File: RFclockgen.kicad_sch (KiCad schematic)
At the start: 13 parts, among them J1 Conn_01x04_Pin, J3 Conn_01x02_Pin, U2 ESP32-S3-WROOM-1, U3 AP2112K-3.3, U4 ESP32-C6-WROOM-1-N8

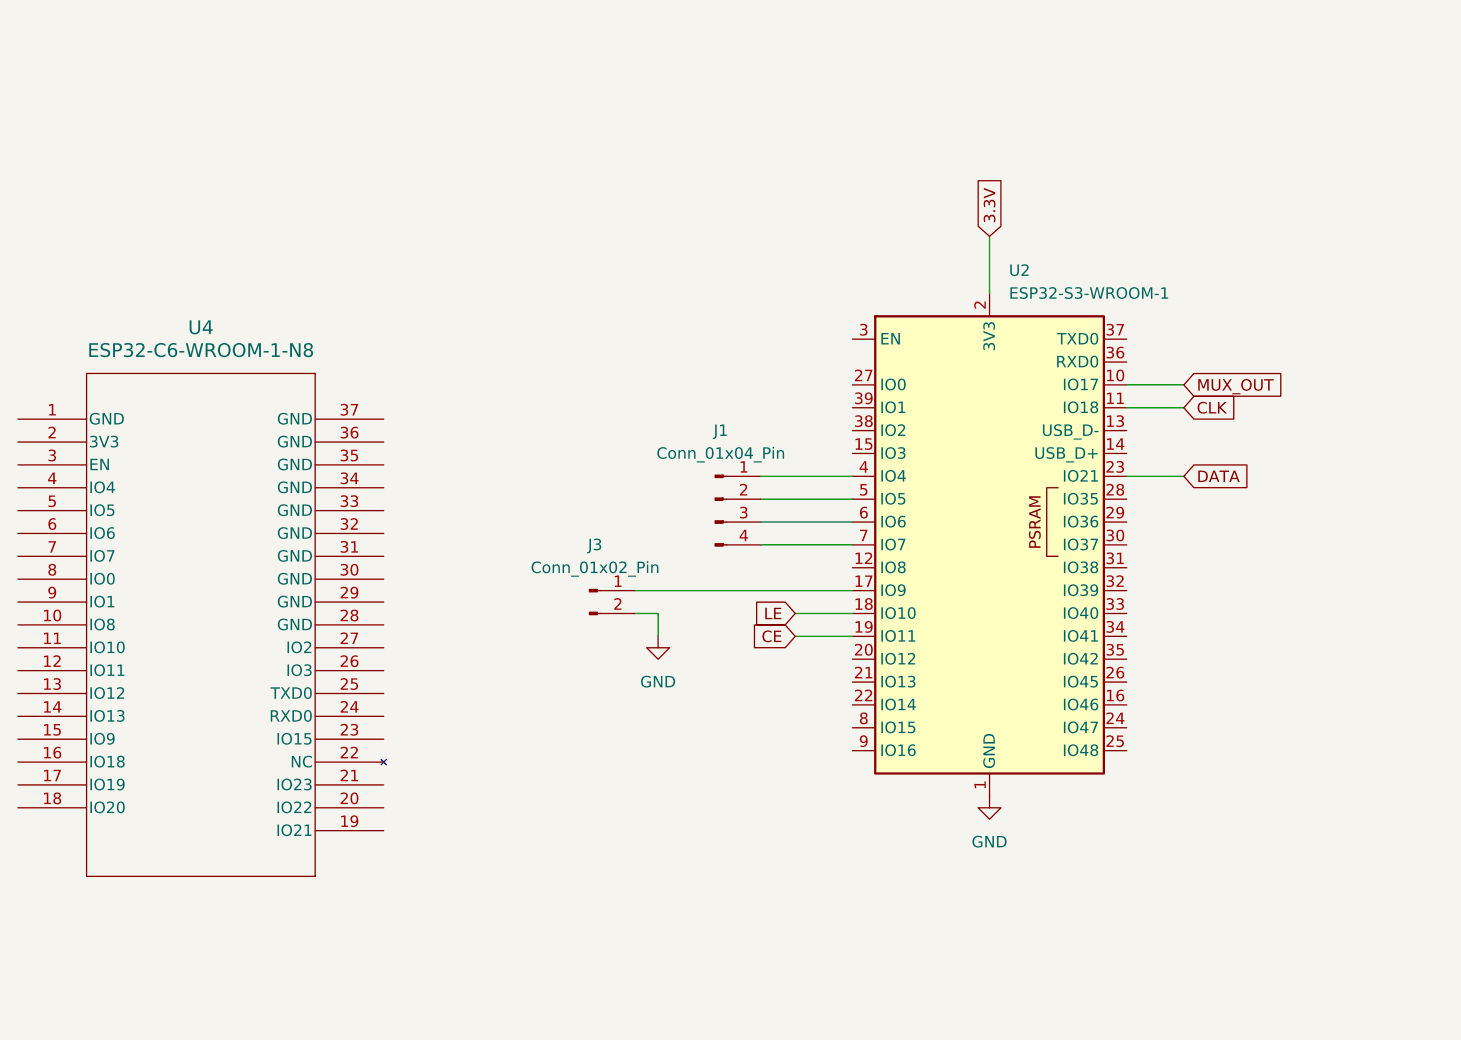
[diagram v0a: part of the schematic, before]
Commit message: Fix: replaced deleted stuff
lost some components in the last merge so this is replacing them
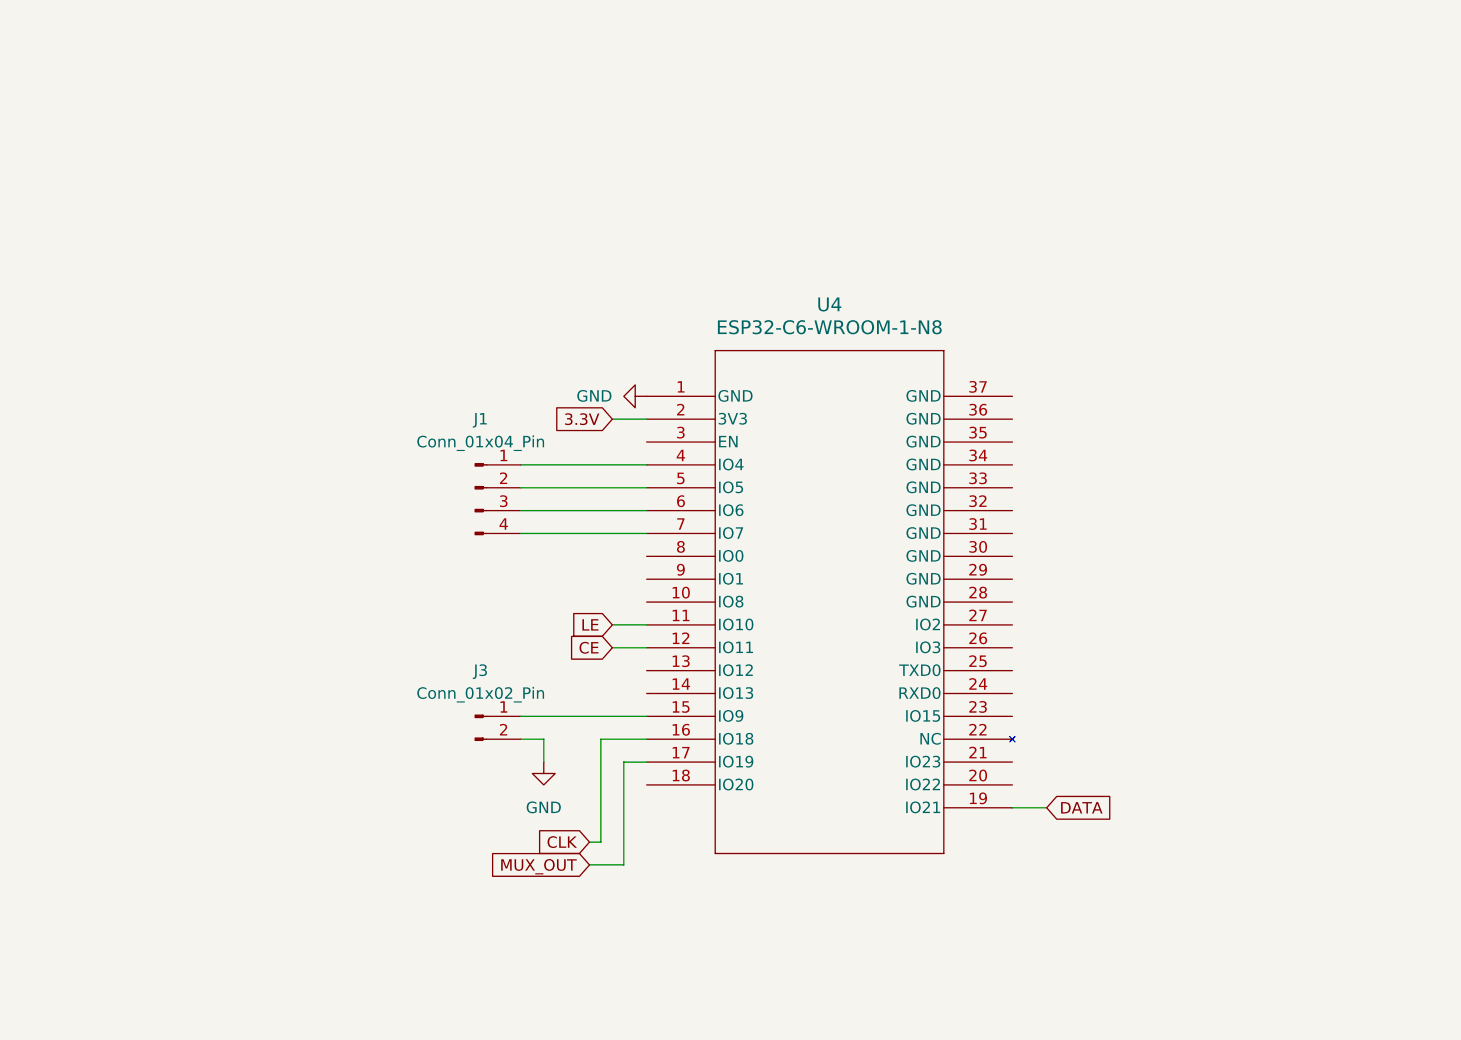
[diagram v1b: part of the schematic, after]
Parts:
- removed U2: ESP32-S3-WROOM-1, RF_Module:ESP32-S3-WROOM-1, symbol RF_Module:ESP32-S3-WROOM-1
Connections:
- net 3.3V: now also U4.2 (3V3)
- net CE: now also U4.12 (IO11)
- net CLK: now also U4.16 (IO18)
- net DATA: now also U4.19 (IO21)
- net GND: now also U4.1 (GND)
- net LE: now also U4.11 (IO10)
- net MUX_OUT: now also U4.17 (IO19)
- net at U4.15 (IO9): now also J3.1 (Pin_1)
- net at U4.4 (IO4): now also J1.1 (Pin_1)
- net at U4.5 (IO5): now also J1.2 (Pin_2)
- net at U4.6 (IO6): now also J1.3 (Pin_3)
- net at U4.7 (IO7): now also J1.4 (Pin_4)
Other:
- moved on the sheet: J1, J3, U4

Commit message: Final update
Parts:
- added C5, C6: 12p, symbol Device:C
- added XTAL1: SIT1552AI-JF-DCC-32.768D, BGA4_SiT1532_SIT, symbol 2026-10-07_02-35-18:SIT1552AI-JF-DCC-32.768D
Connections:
- net GND: now also C5.2, C6.2, XTAL1.1 (GND), XTAL1.4 (GND)
- net EN: now reaches U4.3 (EN)
- net at U4.8 (IO0): now also C6.1, XTAL1.2 (CLK_OUT)
- net at U4.9 (IO1): now also C5.1, XTAL1.3 (VDD)
- net +5V: now reaches C1.1, U3.1 (VIN)
- net +5V: now also U3.3 (EN)
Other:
- added sheet Decoupling capacitors (untitled.kicad_sch)
- moved on the sheet: J1, J3, U4

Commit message: Implemented UART and an Autodownload
Added a Uart Chip and some stuff for the autodownload to make programming easier
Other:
- added sheet AUTODOWNLOAD (AUTODOWNLOAD.kicad_sch)
- added sheet UART (UART.kicad_sch)
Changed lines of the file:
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@@
+	)
+	(sheet
+		(at 379.73 53.34)
+		(size 57.15 27.94)
+		(exclude_from_sim no)
+		(in_bom yes)
+		(on_board yes)
+		(dnp no)
+		(fields_autoplaced yes)
+		(stroke
+			(width 0.1524)
+			(type solid)
+		)
+		(fill
+			(color 0 0 0 0.0000)
+		)
+		(property "Sheetname" "AUTODOWNLOAD"
+			(at 379.73 52.6284 0)
+			(effects
+				(font
+					(size 1.27 1.27)
+				)
+				(justify left bottom)
+			)
+		)
+		(property "Sheetfile" "AUTODOWNLOAD.kicad_sch"
+			(at 379.73 81.8646 0)
+			(effects
+				(font
+					(size 1.27 1.27)
+				)
+				(justify left top)
+			)
+		)
+		(instances
+			(project "RFclockgen"
+				(path "/e1444a2d-a0c4-493c-a136-c624dc084e46"
+					(page "7")
+				)
+			)
+		)
 	)
 	(sheet
@@
 				)
 			)
+		)
+	)
+	(sheet
+		(at 379.73 15.24)
+		(size 57.15 27.94)
+		(exclude_from_sim no)
+		(in_bom yes)
+		(on_board yes)
+		(dnp no)
+		(fields_autoplaced yes)
+		(stroke
+			(width 0.1524)
+			(type solid)
+		)
+		(fill
+			(color 0 0 0 0.0000)
+		)
+		(property "Sheetname" "UART"
+			(at 379.73 14.5284 0)
+			(effects
+				(font
+					(size 1.27 1.27)
+				)
+				(justify left bottom)
+			)
+		)
+		(property "Sheetfile" "UART.kicad_sch"
+			(at 379.73 43.7646 0)
+			(effects
+				(font
+					(size 1.27 1.27)
+				)
+				(justify left top)
+			)
+		)
+		(instances
+			(project "RFclockgen"
+				(path "/e1444a2d-a0c4-493c-a136-c624dc084e46"
+					(page "6")
+				)
+			)
